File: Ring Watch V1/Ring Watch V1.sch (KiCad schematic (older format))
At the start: 15 parts, among them J1 Programming Header, J2 CR2023 Socket, U1 ATtiny85-20SU, U2 PCF8523T, Y1 32.768

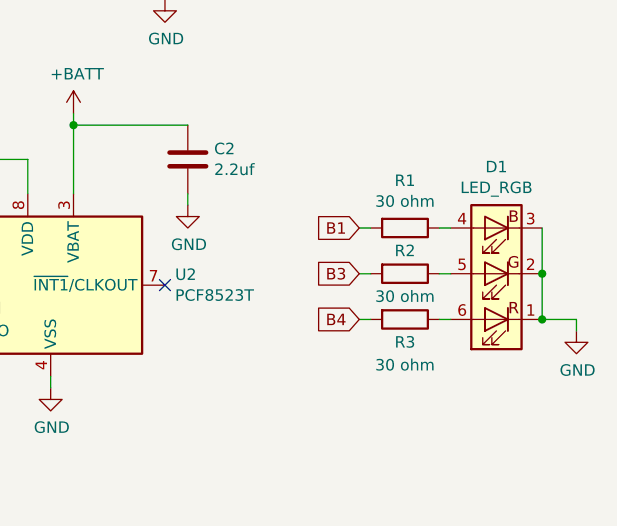
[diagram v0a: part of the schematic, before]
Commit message: rgb calcs, updated Digikey BOM
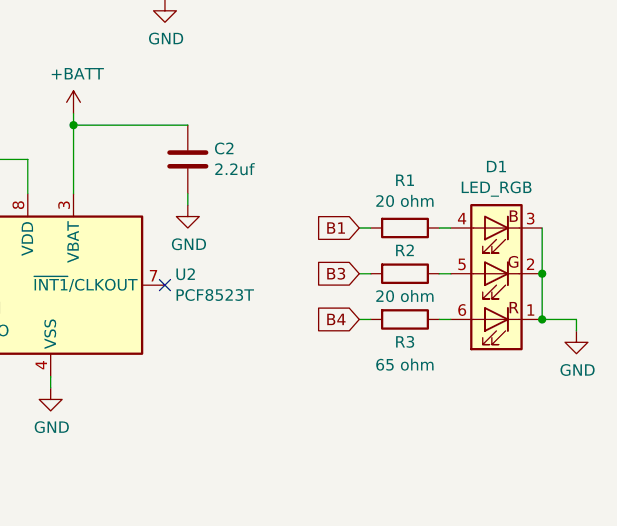
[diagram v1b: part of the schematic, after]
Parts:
- R1, R2: value 30 ohm -> 20 ohm
- R3: value 30 ohm -> 65 ohm
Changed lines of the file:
@@
 P 6300 2550
 F 0 "R1" V 6093 2550 50  0000 C CNN
-F 1 "30 ohm" V 6184 2550 50  0000 C CNN
+F 1 "20 ohm" V 6184 2550 50  0000 C CNN
 F 2 "Resistor_SMD:R_0805_2012Metric_Pad1.15x1.40mm_HandSolder" V 6230 2550 50  0001 C CNN
 F 3 "~" H 6300 2550 50  0001 C CNN
@@
 P 6300 2750
 F 0 "R2" V 6200 2750 50  0000 C CNN
-F 1 "30 ohm" V 6400 2750 50  0000 C CNN
+F 1 "20 ohm" V 6400 2750 50  0000 C CNN
 F 2 "Resistor_SMD:R_0805_2012Metric_Pad1.15x1.40mm_HandSolder" V 6230 2750 50  0001 C CNN
 F 3 "~" H 6300 2750 50  0001 C CNN
@@
 P 6300 2950
 F 0 "R3" V 6400 2950 50  0000 C CNN
-F 1 "30 ohm" V 6500 2950 50  0000 C CNN
+F 1 "65 ohm" V 6500 2950 50  0000 C CNN
 F 2 "Resistor_SMD:R_0805_2012Metric_Pad1.15x1.40mm_HandSolder" V 6230 2950 50  0001 C CNN
 F 3 "~" H 6300 2950 50  0001 C CNN
